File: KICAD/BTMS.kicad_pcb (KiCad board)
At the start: 4 copper layers, 126.2 x 137.4 mm, 314 parts, among them J1 fan, J10 U1COMMS, J11 U2COMMS, J13 IntBTemp, J14 ctrlTemp, J15 12Vout, J16 12Vin, J17 5Vout, J2 mContactor, J3 Tac, J5 ICSP, J7 5Vout, J9 key, Q1 PSMN5R6-100BS, Q10 PSMN5R6-100BS, Q11 DMN65D8L, Q12 DMN65D8L, Q13 FDN340P, Q14 ZXTP2025FTA, Q15 ZXTP2025FTA, Q16 ZXTP2025FTA, Q18 DMN65D8L, Q2 PSMN5R6-100BS, Q3 PSMN5R6-100BS, Q4 DMN65D8L, Q5 DMN65D8L, Q6 DMN65D8L, Q7 DMN65D8L, Q8 PSMN5R6-100BS, Q9 FDN340P, U1 R-78HB12-0.5, U10 A41AS12VDC, U11 A41AS12VDC, U12 A41AS12VDC, U13 A41AS12VDC, U14 A41AS12VDC, U15 NL17SZ74USG, U2 ACS780xLRTR-050B, U3 UCC27201DDAR, U4 FAN3111ESX, U5 HCPL-3120, U6 L7805CV, U7 LTV-817S, U8 dsPIC30F3011-PT, U9 LM62CIM3/NOPB

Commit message: Updated parts list. Updated Gerber files. Updated board to reflect schematic. Tweaked some parts of the schematic.
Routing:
- net GND: vias 416 -> 417
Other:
- board text removed: "ESD"
- board text removed: "Huh, I don't remember making this part a radio?"
- board text removed: "I'm sick and tired of this circuit not working because of EMI"
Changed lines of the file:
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@@
   (general
     (thickness 1.6)
-    (drawings 251)
-    (tracks 2530)
+    (drawings 248)
+    (tracks 2531)
     (zones 0)
     (modules 314)
@@
   )
   (setup
-    (last_trace_width 0.25)
+    (last_trace_width 0.5)
     (user_trace_width 0.5)
     (user_trace_width 1)
@@
       (at (xyz 0 0 0))
       (scale (xyz 1 1 1))
-      (rotate (xyz 0 0 0))
+      (rotate (xyz 0 0 90))
     )
   )
@@
   (gr_line (start 49.022 40.386) (end 49.022 85.598) (layer B.SilkS) (width 0.12))
   (gr_line (start 155.702 40.386) (end 49.022 40.386) (layer B.SilkS) (width 0.12))
-  (gr_text "Huh, I don't remember making this part a radio?" (at 93.726 47.244) (layer F.SilkS)
-    (effects (font (size 1 1) (thickness 0.15)))
-  )
   (gr_text Maybe? (at 88.646 42.926) (layer F.SilkS)
     (effects (font (size 1 1) (thickness 0.15)))
   )
-  (gr_text "I'm sick and tired of this circuit not working because of EMI" (at 74.676 174.498) (layer B.SilkS)
-    (effects (font (size 1 1) (thickness 0.15)) (justify mirror))
-  )
-  (gr_text ESD (at 89.662 51.308) (layer F.SilkS)
-    (effects (font (size 1 1) (thickness 0.15)))
-  )
   (gr_text HOT (at 83.82 42.926) (layer F.SilkS)
     (effects (font (size 1 1) (thickness 0.15)))
@@
   (via (at 85.09 82.55) (size 1) (drill 0.5) (layers F.Cu B.Cu) (net 1))
   (via (at 85.09 78.994) (size 1) (drill 0.5) (layers F.Cu B.Cu) (net 1))
+  (via (at 84.328 150.876) (size 0.8) (drill 0.4) (layers F.Cu B.Cu) (net 1))
   (segment (start 42.672 48.006) (end 40.386 48.006) (width 0.5) (layer F.Cu) (net 2) (status 10))
   (segment (start 109.22 76.708) (end 112.522 76.708) (width 0.5) (layer F.Cu) (net 2) (status 10))

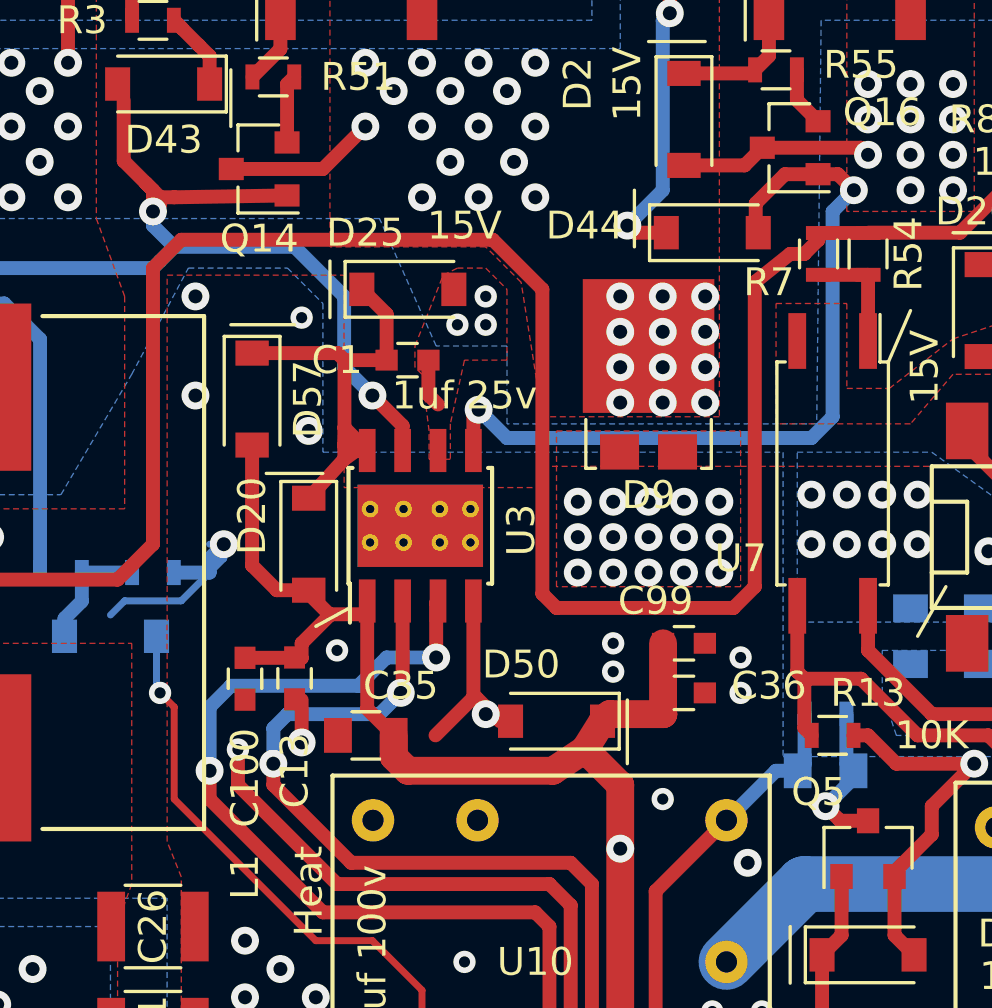
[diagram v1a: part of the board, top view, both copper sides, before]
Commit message: Updated U3 to reflect proper pinout for UCC27201DDAR
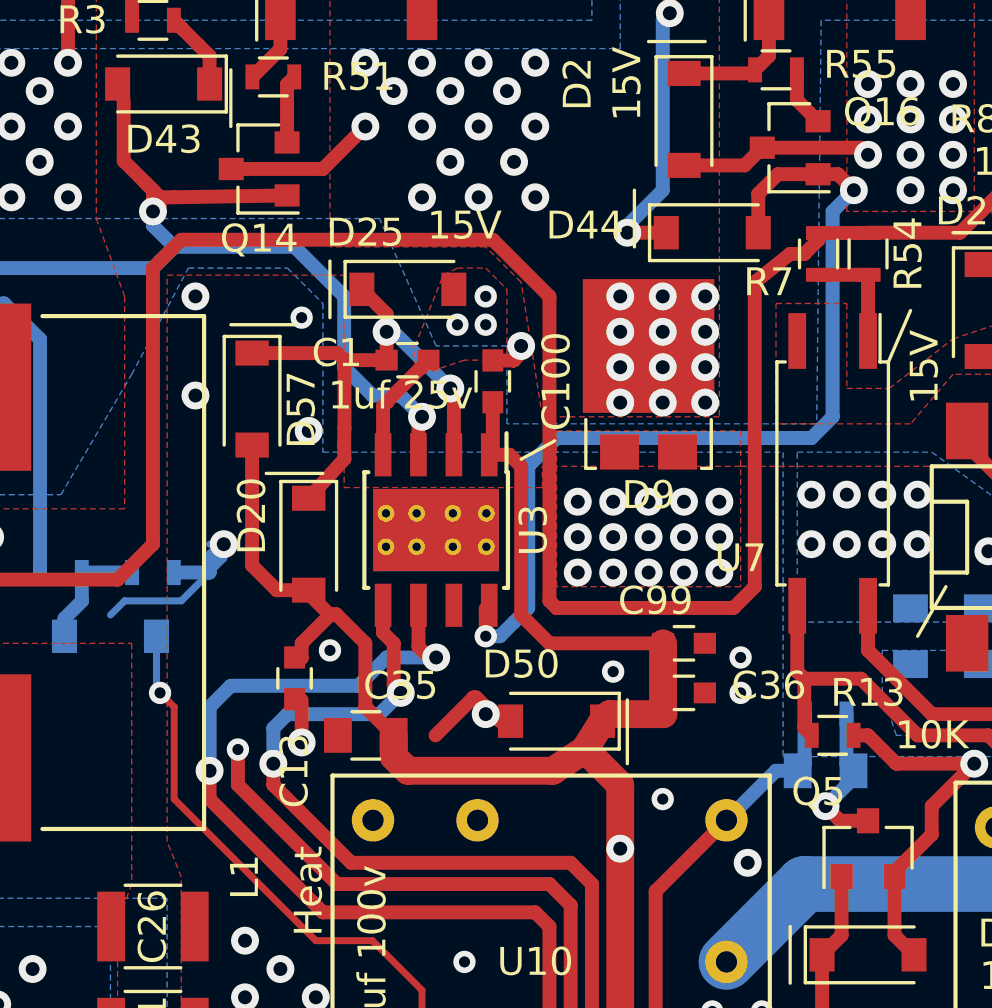
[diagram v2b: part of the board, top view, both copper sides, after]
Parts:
- R5: value 8 -> 6
- moved C100 13.9 mm to (95.8, 82.0), turned to 90 degrees
- moved U3 0.59 mm to (93.7, 87.4), turned to 270 degrees
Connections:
- U3 pad 2: Net-(R59-Pad2) -> Net-(C1-Pad1)
- U3 pad 3: Net-(D60-Pad2) -> Net-(D42-Pad2)
- U3 pad 4: GND -> Net-(C1-Pad2)
- U3 pad 5: Net-(D44-Pad2) -> Net-(R59-Pad2)
- U3 pad 6: Net-(C1-Pad2) -> Net-(D60-Pad2)
- U3 pad 7: Net-(D42-Pad2) -> GND
- U3 pad 8: Net-(C1-Pad1) -> Net-(D44-Pad2)
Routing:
- net +12V: track 402.0 -> 413.4 mm
- net Net-(D44-Pad2): track 28.7 -> 33.6 mm
- net Net-(C1-Pad1): track 16.4 -> 18.8 mm, vias 0 -> 2
- net Net-(C1-Pad2): track 54.5 -> 56.9 mm
- net GND: track 566.2 -> 564.6 mm
- net Net-(D42-Pad2): track 47.8 -> 48.8 mm

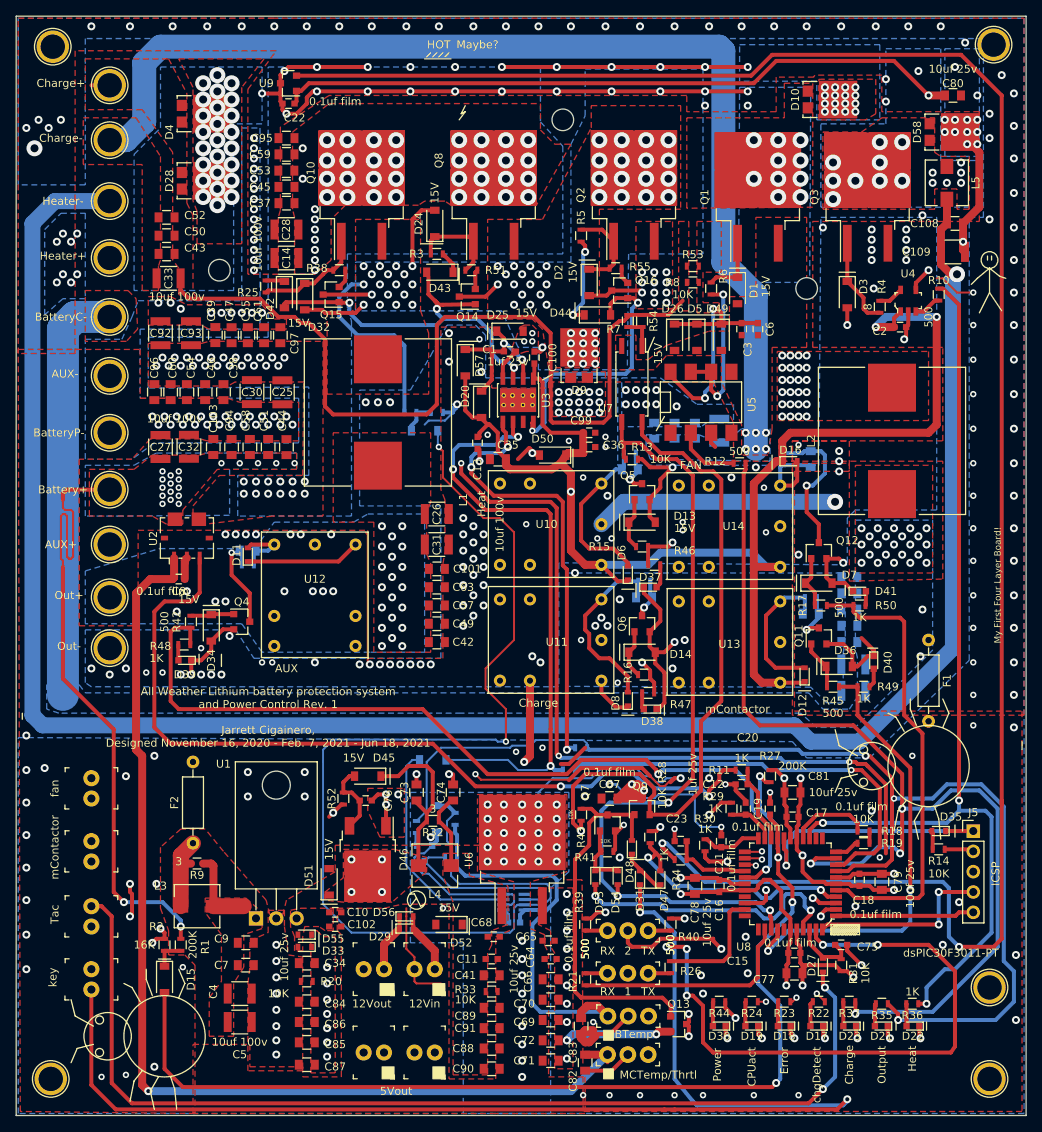
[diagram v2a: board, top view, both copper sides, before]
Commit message: Cleaned up some corners on PCB layout. I don't like the main buck converter half bridge design. Might change later. Still Need To Test This Revision.
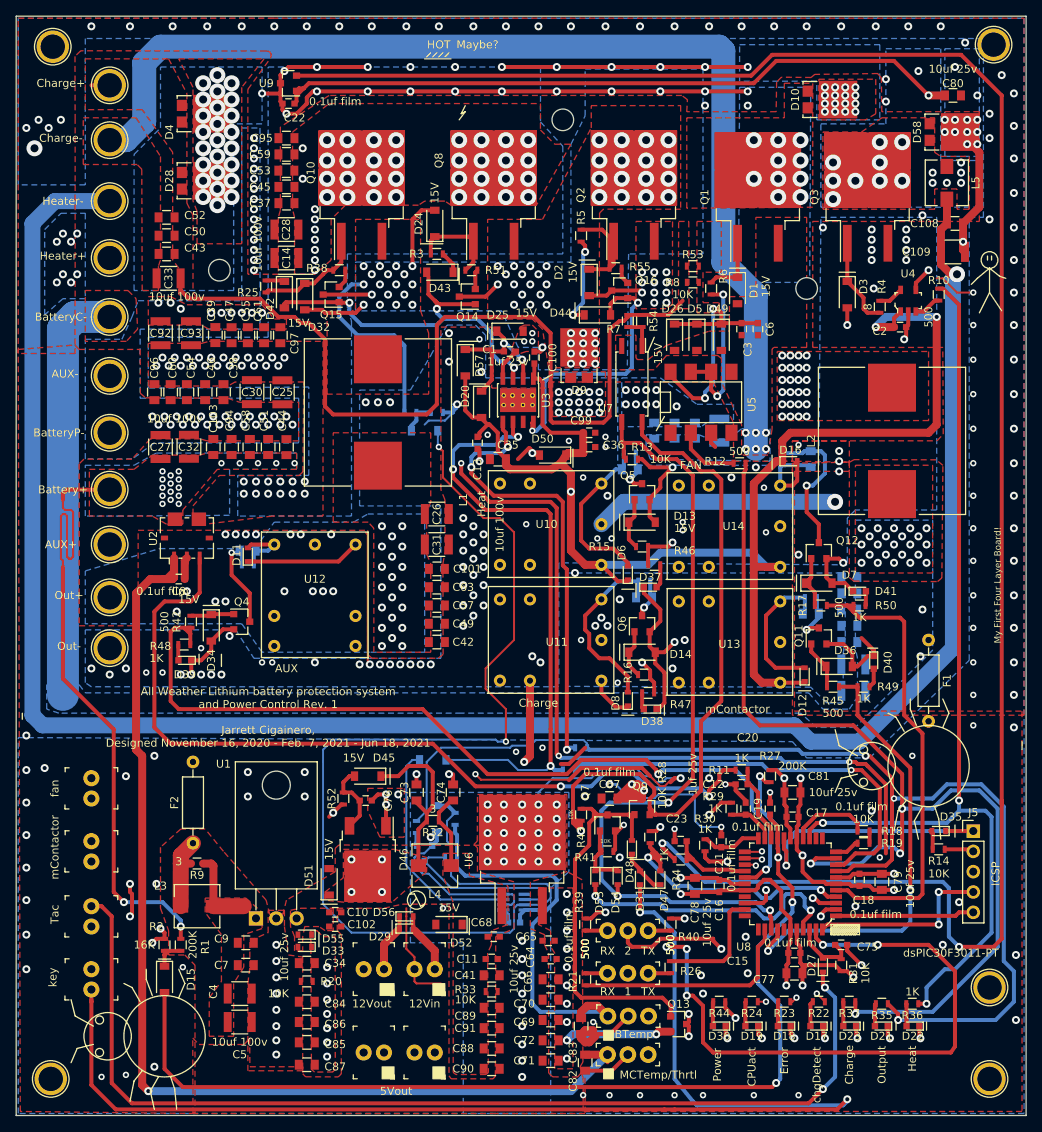
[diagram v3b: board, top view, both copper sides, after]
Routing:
- net +12V: track 413.4 -> 439.4 mm
- net +5V: track 97.2 -> 112.8 mm
- net GND: track 564.6 -> 574.1 mm
- net Net-(D2-Pad1): track 10.8 -> 14.9 mm
- net /IntBus: track 136.7 -> 140.7 mm
- net +5C: track 361.4 -> 364.5 mm
- net /__PwrKey: track 31.7 -> 34.2 mm
- net /M+: track 0.00 -> 1.99 mm
- net Net-(D48-Pad2): track 47.4 -> 48.8 mm
- net Net-(D53-Pad1): track 8.04 -> 9.27 mm
- net /brdTemp: track 10.2 -> 11.3 mm
- net /CoolCTRL: track 57.4 -> 58.5 mm
- net /AUXpower: track 107.3 -> 108.3 mm
- net Net-(D7-Pad1): track 6.63 -> 7.58 mm
- net Net-(D15-Pad1): track 4.04 -> 4.80 mm

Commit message: Cleaned up a few things. Added mosfet to help protect against both high and low side fets from being on at the same time. Generated Gerber Files. Getting ready to fabricate this board and begin testing.
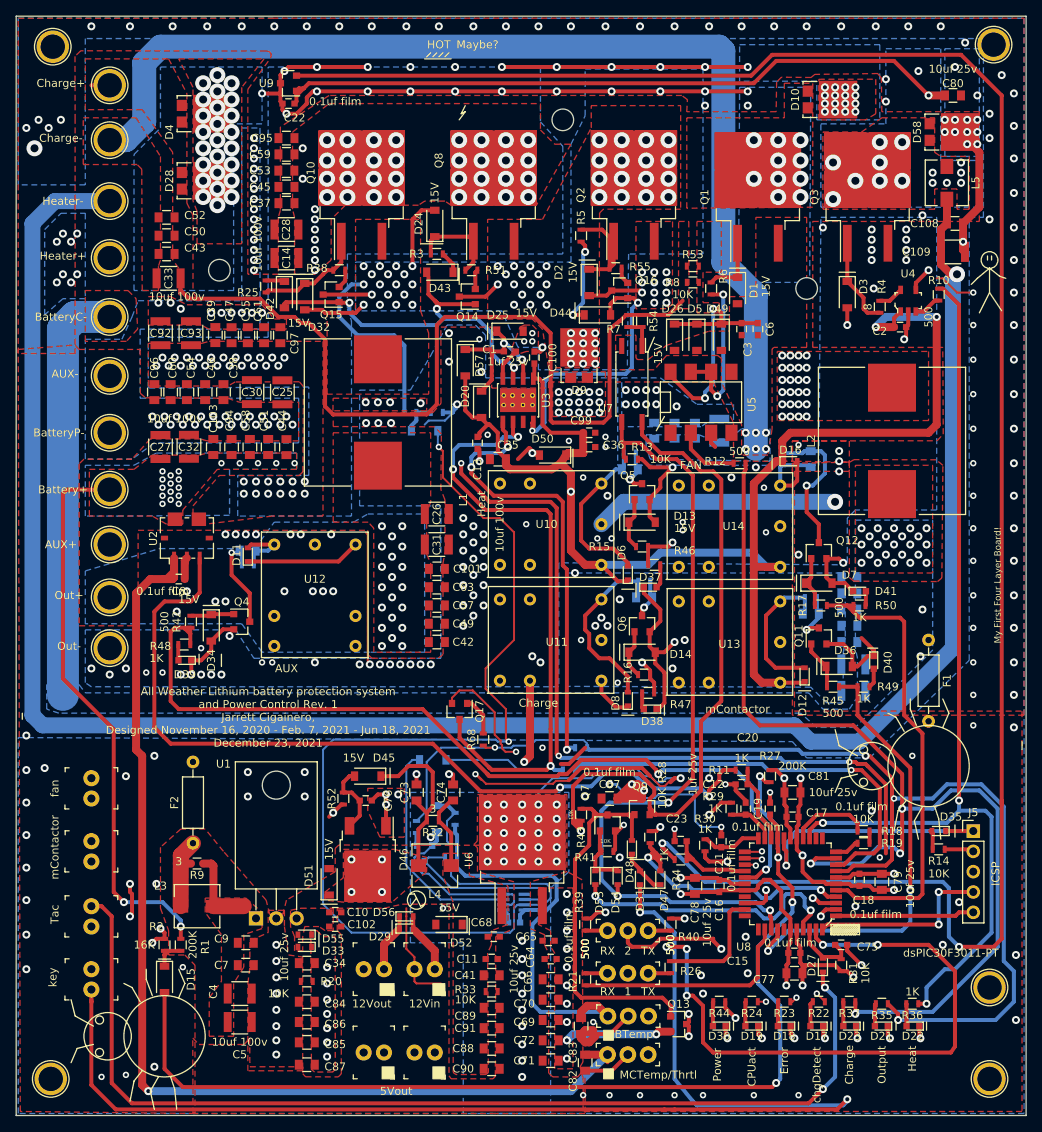
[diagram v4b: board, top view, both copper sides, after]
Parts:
- added Q17: DMN65D8L, TO_SOT_Packages_SMD:SOT-23, F.Cu at (86.4, 126.3)
- added R68: 500, Resistors_SMD:R_0603, F.Cu at (89.4, 129.8)
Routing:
- net GND: track 574.1 -> 589.9 mm, vias 417 -> 421
- net Net-(D60-Pad2): track 75.6 -> 91.1 mm
- net /B+: track 83.8 -> 70.6 mm
- net Net-(Q17-Pad1): track 0.00 -> 4.92 mm
- net /Mctrl+: track 146.3 -> 147.7 mm, vias 3 -> 4
- net Net-(R11-Pad2): track 105.2 -> 105.7 mm
- net Net-(D58-Pad1): vias 15 -> 14
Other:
- board text added: "All Weather Lithium battery protection system and Power Control Rev. 1 Jarrett Cigainero, Designed November 16, 2020 - Feb. 7, 2021 - Jun 18, 2021 December 23, 2021"
- board text removed: "All Weather Lithium battery protection system and Power Control Rev. 1 Jarrett Cigainero, Designed November 16, 2020 - Feb. 7, 2021 - Jun 18, 2021"
